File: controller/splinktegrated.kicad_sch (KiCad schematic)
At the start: 50 parts, among them J1 USB_C_Receptacle_USB2.0, J10 NA_Ribbon, J12 NA_Conn_01x04_Female, J14 Cirque, J2 NA_Conn_01x04_Female, J3 NA_Conn_01x04_Female, J4 NA_Conn_01x04_Female, J5 Conn_01x02, J6 Cirque, J7 NA_trackball, J8 NA_Ribbon, J9 NA_RGB, SW1 NA_SW_SPST, SW2 NA_SW_SPST, U1 RP2040, U3 XC6210B332MR-G, U4 USBLC6-2P6, U5 W25Q128JVS, Y1 Crystal_GND24

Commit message: work
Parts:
- removed J10: NA_Ribbon, Library:5_PinHeader, symbol Connector:Conn_01x05_Female
- removed J12, J4: NA_Conn_01x04_Female, drawings:PinHeader_1x04_P2.54mm_Vertical, symbol Connector:Conn_01x04_Female
- removed J14, J6: Cirque, local-libraries:FPC-SMD_FPC05012-09200-.5mm, symbol Connector:Conn_01x14_Female
- removed J2, J3: NA_Conn_01x04_Female, Library:PinHeader_1x04_P2.54mm_Vertical_USB, symbol Connector:Conn_01x04_Female
- removed J7: NA_trackball, Library:6_PinHeader, symbol Connector:Conn_01x06_Female
- removed J8: NA_Ribbon, Library:6_PinHeader, symbol Connector:Conn_01x06_Female
- removed J9: NA_RGB, Library:header1x03, symbol Connector:Conn_01x03_Female
- removed SW1: NA_SW_SPST, Library:PushSwitch, symbol Switch:SW_SPST
- added J11: Conn_01x07_Socket, Connector_PinSocket_2.54mm:PinSocket_1x07_P2.54mm_Vertical, symbol Connector:Conn_01x07_Socket
- added J7: Cirque, local-libraries:FPC-SMD_FPC05012-09200-.5mm, symbol Connector:Conn_01x14_Female
- H1, H2: footprint Library:MountingHole_4mm_Pad_Via -> drawings:MountingHole_3mm_Pad_Via
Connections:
- net +3V3: now also J7.12 (Pin_12)
- net GND: now also J7.11 (Pin_11)
- net miso_l: now also J7.2 (Pin_2)
- net mosi_l: now also J7.5 (Pin_5)
- net sc_l: now also J7.1 (Pin_1)
- net col1_l renamed A1
- net col2_l renamed A2
- net col3_l renamed NCS
- net NCS: now also J7.3 (Pin_3)
- net col4_l renamed D6
- net col5_l renamed D7
- net col6_l renamed D8
- net rgb_r renamed D0
- net row1_l renamed A3
- net row2_l renamed A0
- net row3_l renamed D5
- net row4_l renamed D4
- net row5_l renamed D9
- net serial_l renamed D1
- net split_hand_l renamed D15
- net ss_l renamed D16
- no-connect marks 19 -> 22
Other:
- note added: "Cirque FPC connector"
- note removed: "Headers"
- note removed: "RowCol FPC Connector"
- note removed: "Trackball FPC Connector"

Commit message: work
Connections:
- net D6 is gone; now on net sw1: U1.8 (GPIO6)
- net D7 is gone; now on net sw2: U1.9 (GPIO7)
- net D8 is gone; now on net sw3: U1.11 (GPIO8)
- net D9 is gone; now on net sw4: U1.12 (GPIO9)
- net sw1: now reaches J11.1 (Pin_1)
- net sw2: now reaches J11.2 (Pin_2)
- net sw3: now reaches J11.3 (Pin_3)
- net sw4: now reaches J11.4 (Pin_4)
- net A0: no longer names the net of U1.38 (GPIO26_ADC0)
- net A1: no longer names the net of U1.39 (GPIO27_ADC1)
- net A2: no longer names the net of U1.40 (GPIO28_ADC2)
- net A3: no longer names the net of U1.41 (GPIO29_ADC3)
- net D0: no longer names the net of U1.2 (GPIO0)
- net D1: no longer names the net of U1.3 (GPIO1)
- net D15: no longer names the net of U1.18 (GPIO15)
- net D16: no longer names the net of U1.27 (GPIO16)
- net D4: no longer names the net of U1.6 (GPIO4)
- net D5: no longer names the net of U1.7 (GPIO5)
- no-connect marks 22 -> 32
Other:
- moved on the sheet: J11, J7

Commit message: work
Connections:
- net +3V3: now also J11.7 (Pin_7)
- net GND: now also J11.5 (Pin_5)
- net RGB: now reaches U1.13 (GPIO10)
- net RGB: now also J11.6 (Pin_6)
- no-connect marks 32 -> 31
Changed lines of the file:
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@@
 	)
 	(no_connect
-		(at 182.88 83.82)
-	)
-	(no_connect
 		(at 182.88 104.14)
 	)
@@
 		)
 	)
+	(global_label "RGB"
+		(shape input)
+		(at 299.72 45.72 180)
+		(effects
+			(font
+				(size 1.27 1.27)
+			)
+			(justify right)
+		)
+		(property "Intersheetrefs" "${INTERSHEET_REFS}"
+			(at 295.1902 45.6406 0)
+			(effects
+				(font
+					(size 1.27 1.27)
+				)
+				(justify right)
+				(hide yes)
+			)
+		)
+	)
 	(global_label "NCS"
 		(shape input)
@@
 		)
 	)
+	(global_label "RGB"
+		(shape input)
+		(at 182.88 83.82 0)
+		(effects
+			(font
+				(size 1.27 1.27)
+			)
+			(justify left)
+		)
+		(property "Intersheetrefs" "${INTERSHEET_REFS}"
+			(at 187.4098 83.8994 0)
+			(effects
+				(font
+					(size 1.27 1.27)
+				)
+				(justify left)
+				(hide yes)
+			)
+		)
+	)
 	(global_label "miso_l"
 		(shape input)
@@
 	)
 	(symbol
+		(lib_id "power:GND")
+		(at 299.72 43.18 270)
+		(unit 1)
+		(exclude_from_sim no)
+		(in_bom yes)
+		(on_board yes)
+		(dnp no)
+		(property "Reference" "#PWR03"
+			(at 293.37 43.18 0)
+			(effects
+				(font
+					(size 1.27 1.27)
+				)
+				(hide yes)
+			)
+		)
+		(property "Value" "GND"
+			(at 295.91 43.18 0)
+			(effects
+				(font
+					(size 1.27 1.27)
+				)
+			)
+		)
+		(property "Footprint" ""
+			(at 299.72 43.18 0)
+			(effects
+				(font
+					(size 1.27 1.27)
+				)
+				(hide yes)
+			)
+		)
+		(property "Datasheet" ""
+			(at 299.72 43.18 0)
+			(effects
+				(font
+					(size 1.27 1.27)
+				)
+				(hide yes)
+			)
+		)
+		(property "Description" ""
+			(at 299.72 43.18 0)
+			(effects
+				(font
+					(size 1.27 1.27)
+				)
+				(hide yes)
+			)
+		)
+		(pin "1"
+		)
+		(instances
+			(project "splinktegrated"
+				(path "/7353e96a-343a-4876-b497-b1d205a14d97"
+					(reference "#PWR03")
+					(unit 1)
+				)
+			)
+		)
+	)
+	(symbol
 		(lib_id "Device:R")
 		(at 120.65 93.98 90)
@@
 					(unit 1)
 				)
+			)
+		)
+	)
+	(symbol
+		(lib_id "power:+3.3V")
+		(at 299.72 48.26 90)
+		(unit 1)
+		(exclude_from_sim no)
+		(in_bom yes)
+		(on_board yes)
+		(dnp no)
+		(property "Reference" "#PWR07"
+			(at 303.53 48.26 0)
+			(effects
+				(font
+					(size 1.27 1.27)
+				)
+				(hide yes)
+			)
+		)
+		(property "Value" "+3V3"
+			(at 295.91 48.26 0)
+			(effects
+				(font
+					(size 1.27 1.27)
+				)
+			)
+		)
+		(property "Footprint" ""
+			(at 299.72 48.26 0)
+			(effects
+				(font
+					(size 1.27 1.27)
+				)
+				(hide yes)
+			)
+		)
+		(property "Datasheet" ""
+			(at 299.72 48.26 0)
+			(effects
+				(font
+					(size 1.27 1.27)
+				)
+				(hide yes)
+			)
+		)
+		(property "Description" ""
+			(at 299.72 48.26 0)
+			(effects
+				(font
+					(size 1.27 1.27)
+				)
+				(hide yes)
+			)
+		)
+		(pin "1"
+		)
+		(instances
+			(project "splinktegrated"
+				(path "/7353e96a-343a-4876-b497-b1d205a14d97"
+					(reference "#PWR07")
+					(unit 1)
+				)

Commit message: work
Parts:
- J11: footprint Connector_PinSocket_2.54mm:PinSocket_1x07_P2.54mm_Vertical -> Library:PinSocket_1x07_P2.54mm_Vertical
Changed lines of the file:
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@@
 			)
 		)
-		(property "Footprint" "Connector_PinSocket_2.54mm:PinSocket_1x07_P2.54mm_Vertical"
+		(property "Footprint" "Library:PinSocket_1x07_P2.54mm_Vertical"
 			(at 304.8 40.64 0)
 			(effects

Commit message: VIK
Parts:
- added J2: Conn_01x04_Socket, Connector_PinSocket_2.54mm:PinSocket_1x04_P2.54mm_Vertical, symbol Connector:Conn_01x04_Socket
- added JP1: Jumper_2_Bridged, Jumper:SolderJumper-2_P1.3mm_Open_RoundedPad1.0x1.5mm, symbol Jumper:Jumper_2_Bridged
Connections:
- net sc_l is gone; now on net SCLK: J7.1 (Pin_1), U1.34 (GPIO22)
- net +3V3: now also JP1.1 (A)
- net NCS: now also U1.16 (GPIO13); no longer U1.32 (GPIO21)
- net RGB: now also J7.8 (Pin_8), U1.37 (GPIO25); no longer U1.13 (GPIO10)
- net SCL: now reaches U1.14 (GPIO11)
- net SCL: now also J7.9 (Pin_9), J2.2 (Pin_2)
- net MISO: now reaches U1.15 (GPIO12)
- net MISO: now also J7.2 (Pin_2)
- net SCLK: now reaches U1.17 (GPIO14)
- net MOSI: now reaches U1.18 (GPIO15)
- net MOSI: now also J7.5 (Pin_5)
- net A0: now reaches U1.38 (GPIO26_ADC0)
- net A0: now also J7.6 (Pin_6), J2.3 (Pin_3)
- net A1: now reaches U1.39 (GPIO27_ADC1)
- net A1: now also J7.4 (Pin_4), J2.4 (Pin_4)
- net SDA: now reaches J7.10 (Pin_10)
- net SDA: now also U1.13 (GPIO10), J2.1 (Pin_1)
- net at J7.7 (Pin_7): now also JP1.2 (B)
- net miso_l: no longer names the net of U1.31 (GPIO20)
- net miso_l: no longer J7.2 (Pin_2)
- net mosi_l: no longer names the net of U1.35 (GPIO23)
- net mosi_l: no longer J7.5 (Pin_5)
- no-connect marks 31 -> 15
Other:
- note added: "THT breakout"

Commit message: work
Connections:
- net A0 renamed GP26
- net A1 renamed GP27
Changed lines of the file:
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@@
 		)
 	)
-	(label "A0"
+	(label "GP26"
 		(at 353.06 53.34 180)
 		(fields_autoplaced yes)
@@
 		)
 	)
-	(label "A1"
+	(label "GP27"
 		(at 182.88 129.54 0)
 		(fields_autoplaced yes)
@@
 		)
 	)
-	(label "A0"
+	(label "GP26"
 		(at 182.88 127 0)
 		(fields_autoplaced yes)
@@
 		)
 	)
-	(label "A1"
+	(label "GP27"
 		(at 353.06 58.42 180)
 		(fields_autoplaced yes)
@@
 		)
 	)
-	(label "A1"
+	(label "GP27"
 		(at 391.16 43.18 180)
 		(fields_autoplaced yes)
@@
 		)
 	)
-	(label "A0"
+	(label "GP26"
 		(at 391.16 40.64 180)
 		(fields_autoplaced yes)

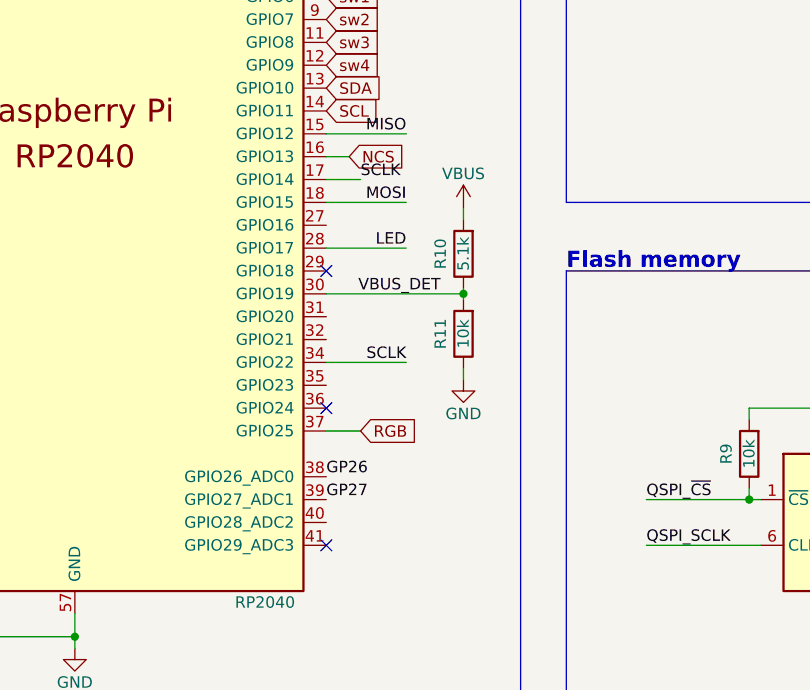
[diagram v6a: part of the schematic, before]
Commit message: remove vbus detect
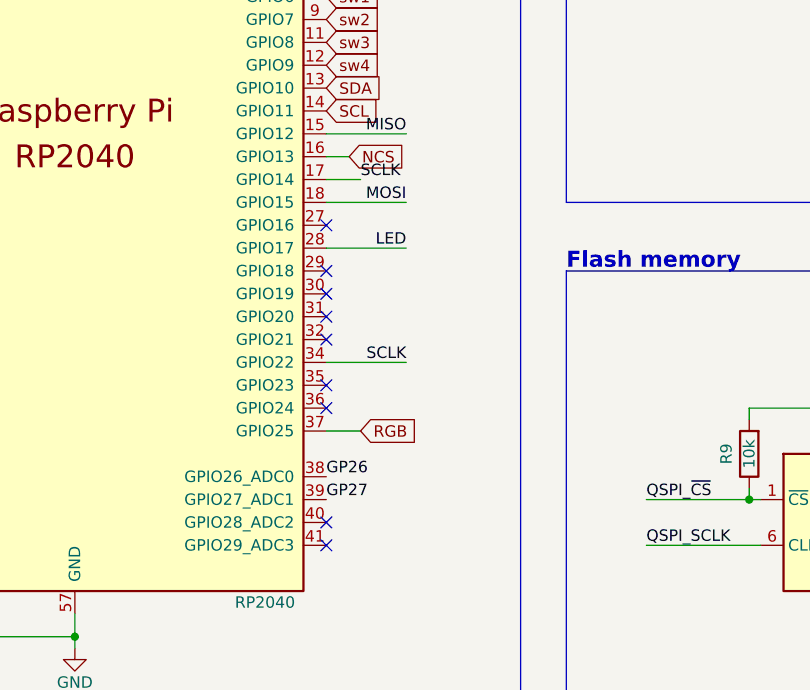
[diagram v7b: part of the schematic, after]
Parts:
- removed R10: 5.1k, Resistor_SMD:R_0402_1005Metric, symbol Device:R
- removed R11: 10k, Resistor_SMD:R_0402_1005Metric, symbol Device:R
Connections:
- net VBUS_DET: no longer names the net of U1.30 (GPIO19)
- no-connect marks 15 -> 21

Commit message: work
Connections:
- net SCLK: no longer U1.17 (GPIO14)
- no-connect marks 21 -> 22
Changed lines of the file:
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@@
+	)
+	(no_connect
+		(at 182.88 93.98)
 	)
 	(no_connect
@@
 		(pts
 			(xy 209.55 104.14) (xy 209.55 158.75)
-		)
-		(stroke
-			(width 0)
-			(type default)
-		)
-	)
-	(wire
-		(pts
-			(xy 182.88 93.98) (xy 186.69 93.98)
 		)
 		(stroke
@@
 		(fields_autoplaced yes)
 		(effects
-			(font
-				(size 1.27 1.27)
-			)
-			(justify left bottom)
-		)
-	)
-	(label "SCLK"
-		(at 186.69 93.98 0)
-		(fields_autoplaced yes)
-		(effects
